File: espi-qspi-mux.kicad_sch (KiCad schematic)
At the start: 6 parts, among them U25 TS3A27518E_QFN

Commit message: Update naming on schematics, fix OSM page size
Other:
- title: BMC Reference Carrier Board -> DC-SCM Carrier Card for OSM-L SoMs
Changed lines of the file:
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@@
 	(paper "A3")
 	(title_block
-		(title "BMC Reference Carrier Board")
-		(date "2025-10-13")
+		(title "DC-SCM Carrier Card for OSM-L SoMs")
+		(date "2025-10-14")
 		(rev "1.1.0")
 	)

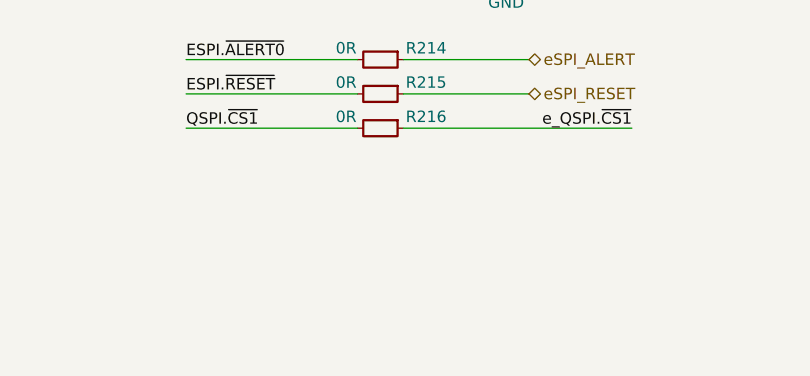
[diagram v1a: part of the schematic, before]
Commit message: Add testpoints to QSPI, Clean DRC
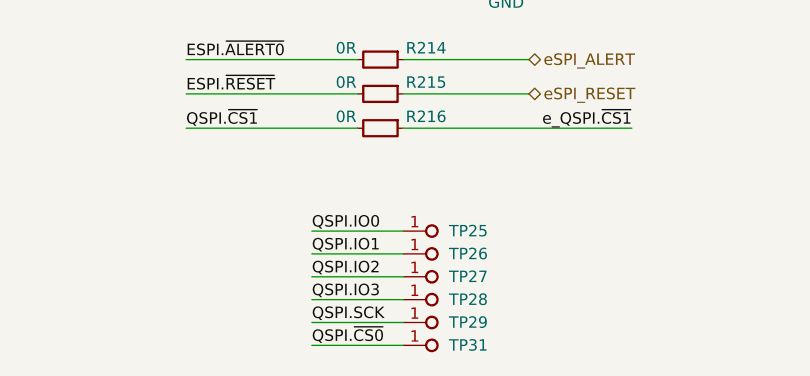
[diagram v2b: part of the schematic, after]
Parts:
- added TP25, TP26, TP27, TP28, TP29, TP31: TP_0.75mm_SMD, antmicro-footprints:TP_SMD_0.75mm, symbol antmicroTestPoints:TP_0.75mm_SMD
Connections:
- net QSPI.IO0: now also TP25.1
- net QSPI.IO1: now also TP26.1
- net QSPI.IO2: now also TP27.1
- net QSPI.IO3: now also TP28.1
- net QSPI.SCK: now also TP29.1
- net QSPI.~{CS0}: now also TP31.1

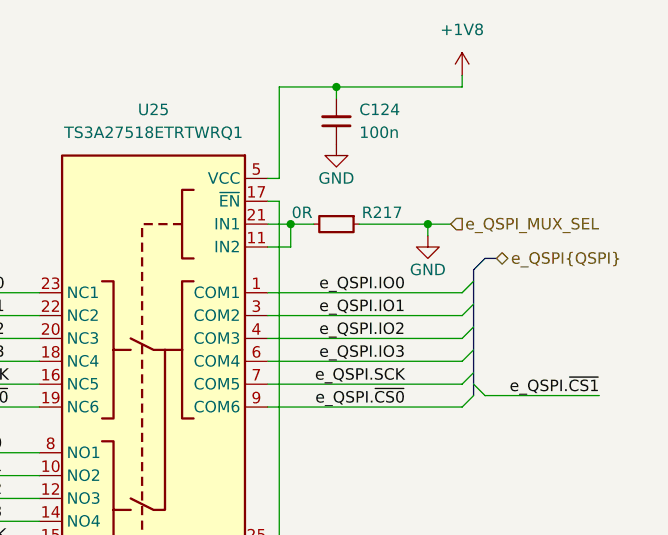
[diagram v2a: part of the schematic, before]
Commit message: Fix missing connections. Clean ERC
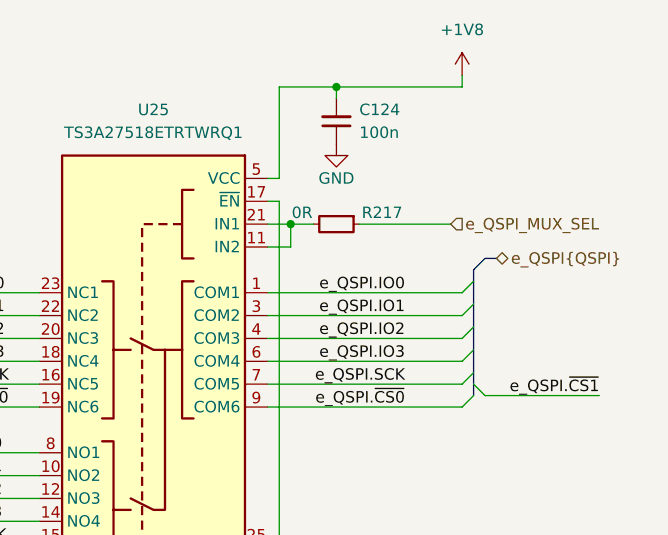
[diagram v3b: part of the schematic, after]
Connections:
- net GND: no longer R217.1
- new net e_QSPI_MUX_SEL: R217.1
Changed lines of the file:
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@@
-	)
-	(junction
-		(at 243.84 124.46)
-		(diameter 0)
-		(color 0 0 0 0)
 	)
 	(junction
@@
 		)
 	)
-	(wire
-		(pts
-			(xy 243.84 124.46) (xy 243.84 125.73)
-		)
-		(stroke
-			(width 0)
-			(type default)
-		)
-	)
 	(bus
 		(pts
@@
 	(wire
 		(pts
-			(xy 243.84 124.46) (xy 236.22 124.46)
+			(xy 236.22 124.46) (xy 246.38 124.46)
 		)
 		(stroke
@@
 		(pts
 			(xy 233.68 109.22) (xy 233.68 110.49)
-		)
-		(stroke
-			(width 0)
-			(type default)
-		)
-	)
-	(wire
-		(pts
-			(xy 246.38 124.46) (xy 243.84 124.46)
 		)
 		(stroke
@@
 					(unit 1)
 				)
-			)
-		)
-	)
-	(symbol
-		(lib_id "antmicropower:GND")
-		(at 243.84 125.73 0)
-		(mirror y)
-		(unit 1)
-		(exclude_from_sim no)
-		(in_bom yes)
-		(on_board yes)
-		(dnp no)
-		(property "Reference" "#PWR0430"
-			(at 234.95 128.27 0)
-			(effects
-				(font
-					(size 1.27 1.27)
-					(thickness 0.15)
-				)
-				(justify left bottom)
-				(hide yes)
-			)
-		)
-		(property "Value" "GND"
-			(at 243.84 129.54 0)
-			(effects
-				(font
-					(size 1.27 1.27)
-					(thickness 0.15)
-				)
-			)
-		)
-		(property "Footprint" ""
-			(at 234.95 133.35 0)
-			(effects
-				(font
-					(size 1.27 1.27)
-					(thickness 0.15)
-				)
-				(justify left bottom)
-				(hide yes)
-			)
-		)
-		(property "Datasheet" ""
-			(at 234.95 138.43 0)
-			(effects
-				(font
-					(size 1.27 1.27)
-					(thickness 0.15)
-				)
-				(justify left bottom)
-				(hide yes)
-			)
-		)
-		(property "Description" ""
-			(at 243.84 125.73 0)
-			(effects
-				(font
-					(size 1.27 1.27)
-				)
-				(hide yes)
-			)
-		)
-		(property "Author" "Antmicro"
-			(at 234.95 133.35 0)
-			(effects
-				(font
-					(size 1.27 1.27)
-					(thickness 0.15)
-				)
-				(justify left bottom)
-				(hide yes)
-			)
-		)
-		(property "License" "Apache-2.0"
-			(at 234.95 135.89 0)
-			(effects
-				(font
-					(size 1.27 1.27)
-					(thickness 0.15)
-				)
-				(justify left bottom)
-				(hide yes)
-			)
-		)
-		(pin "1"
-		)
-		(instances
-			(project "bmc-reference-carrier-board"
-				(path "/5f636c45-3c15-4731-8931-4625e0dab7e4/e532ae7c-55b4-427b-a317-9e407e1b3e94"
-					(reference "#PWR0430")
-					(unit 1)
-				)
